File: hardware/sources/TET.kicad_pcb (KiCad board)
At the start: 4 copper layers, 90.2 x 95.9 mm, 95 parts, among them J1 SWD, M1 MountingHole, M2 MountingHole, M3 MountingHole, M4 MountingHole, U1 TCAN330GDCNR, U10 TLV75533PDBVR, U11 SMA_1, U12 W25Q128JVSIQTR, U13 W25Q128JVSIQTR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

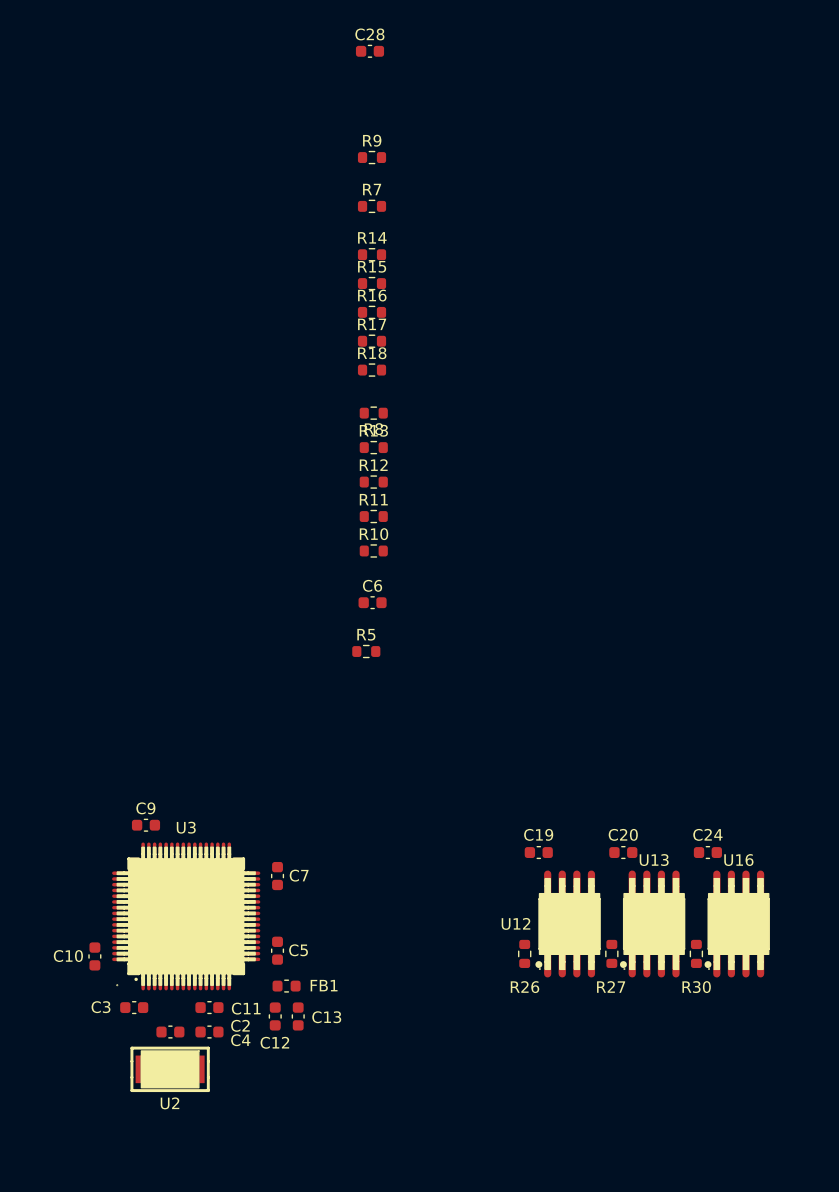
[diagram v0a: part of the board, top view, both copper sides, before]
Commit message: hardware(pcb_design): MCU components placement
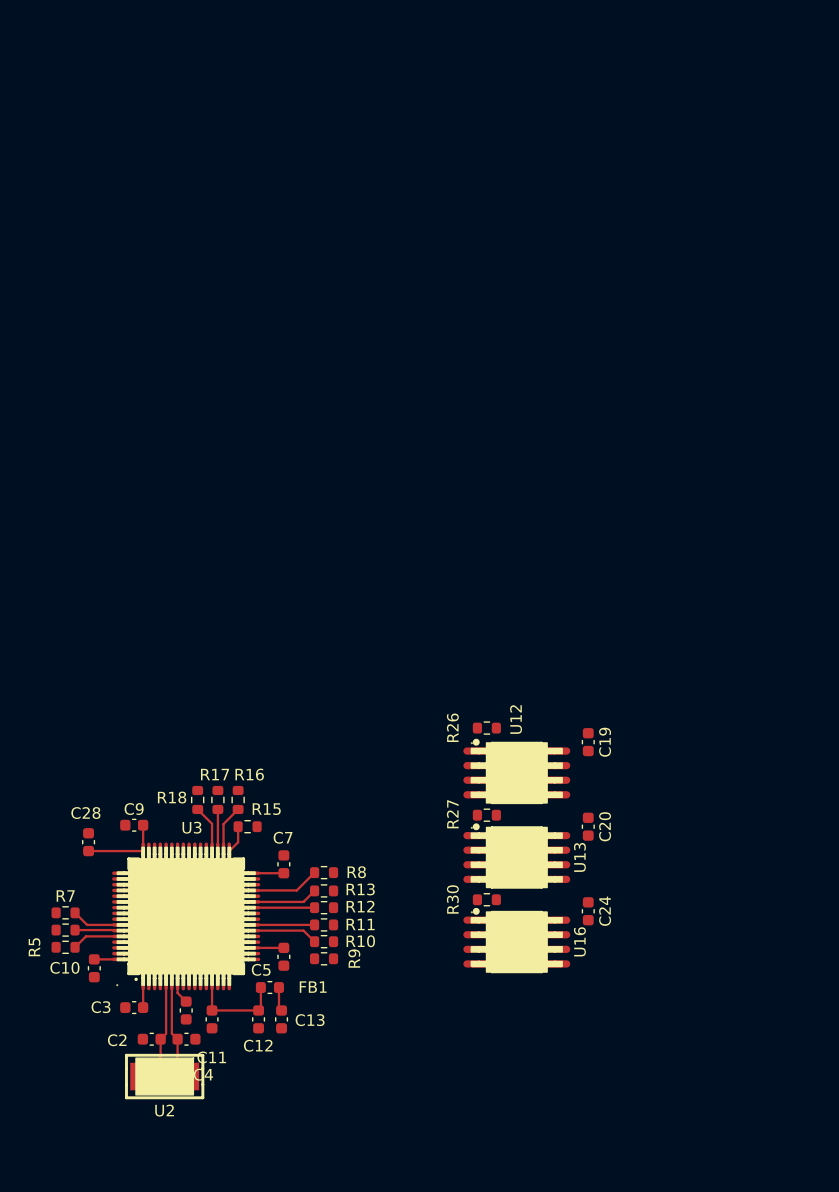
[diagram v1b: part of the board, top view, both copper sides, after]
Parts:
- moved C28 73.1 mm to (3.05, 89.5), turned to 90 degrees
- moved R9 69.9 mm to (23.6, 99.7)
- moved R7 67.0 mm to (1.05, 95.7)
- moved R14 64.6 mm to (1.05, 97.2)
- moved R15 48.5 mm to (16.9, 88.2), turned to 180 degrees
- moved R16 44.0 mm to (16.1, 85.8), turned to -90 degrees
- moved R17 42.1 mm to (14.3, 85.8), turned to -90 degrees
- moved R18 40.4 mm to (12.6, 85.8), turned to -90 degrees
- moved R8 40.2 mm to (23.6, 92.2)
- moved C6 39.0 mm to (11.6, 104.2), turned to -90 degrees
- moved R13 38.8 mm to (23.6, 93.8)
- moved R12 37.3 mm to (23.6, 95.2)
- moved R5 36.7 mm to (1.05, 98.7)
- moved R11 35.8 mm to (23.6, 96.7)
- moved R10 34.3 mm to (23.6, 98.2)
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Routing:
- net +3.3V: track 7.76 -> 27.1 mm
- net Net-(U2-OSC2): track 0.00 -> 9.15 mm
- net Net-(U2-OSC1): track 0.00 -> 8.84 mm
- net +3.3VA: track 0.00 -> 8.63 mm
- net /I2C2_SCL: track 0.00 -> 6.12 mm
- net Net-(U3-PA6): track 0.00 -> 5.87 mm
- net Net-(U3-PB1): track 0.00 -> 5.87 mm
- net Net-(U3-PB0): track 0.00 -> 5.48 mm
- net Net-(U3-PA7): track 0.00 -> 5.48 mm
- net /I2C1_SCL: track 0.00 -> 4.41 mm
- net Net-(U3-PH3/BOOT0): track 0.00 -> 4.37 mm
- net /FLASH2_CS: track 0.00 -> 4.15 mm
- net /FLASH3_CS: track 0.00 -> 4.14 mm
- net /I2C1_SDA: track 0.00 -> 4.00 mm
- net /I2C2_SDA: track 0.00 -> 3.63 mm
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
